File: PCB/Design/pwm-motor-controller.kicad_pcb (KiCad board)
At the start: 2 copper layers, 39 x 53.8 mm, 36 parts, among them J1 Screw_Terminal_01x02, J10 Conn_01x01, J2 Conn_01x01, J3 Conn_01x01, J4 Conn_01x01, J5 Conn_01x01, J6 Conn_01x01, J7 Conn_01x01, J8 Conn_01x01, J9 Conn_01x01, M1 Motor_DC, Q2 NMOS, Q3 MMBT2222A, Q4 Si2319CDS, Q5 NMOS, Q6 MMBT2222A, U1 LMC555xM

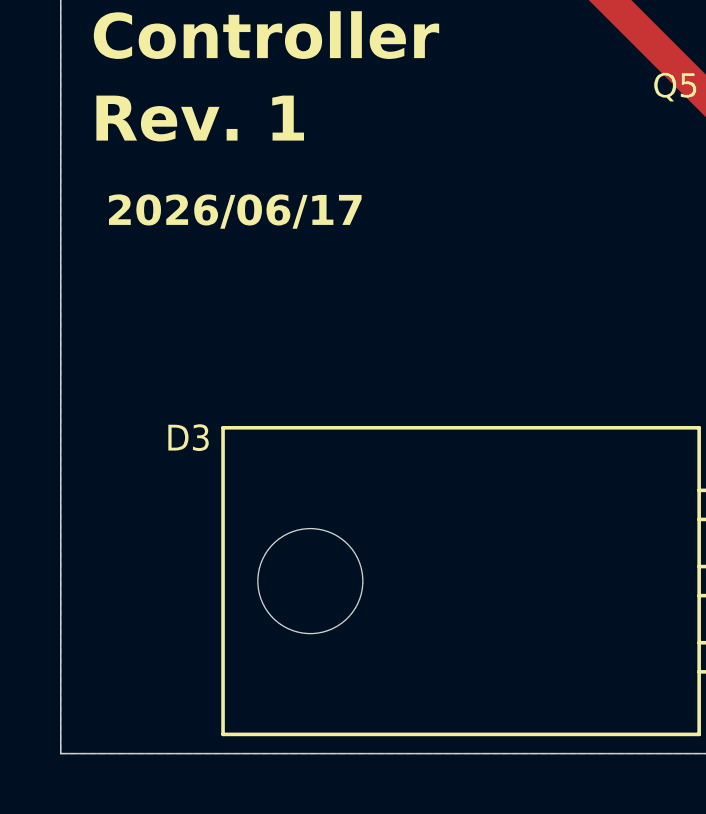
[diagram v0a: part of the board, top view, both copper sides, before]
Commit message: Added mounting holes
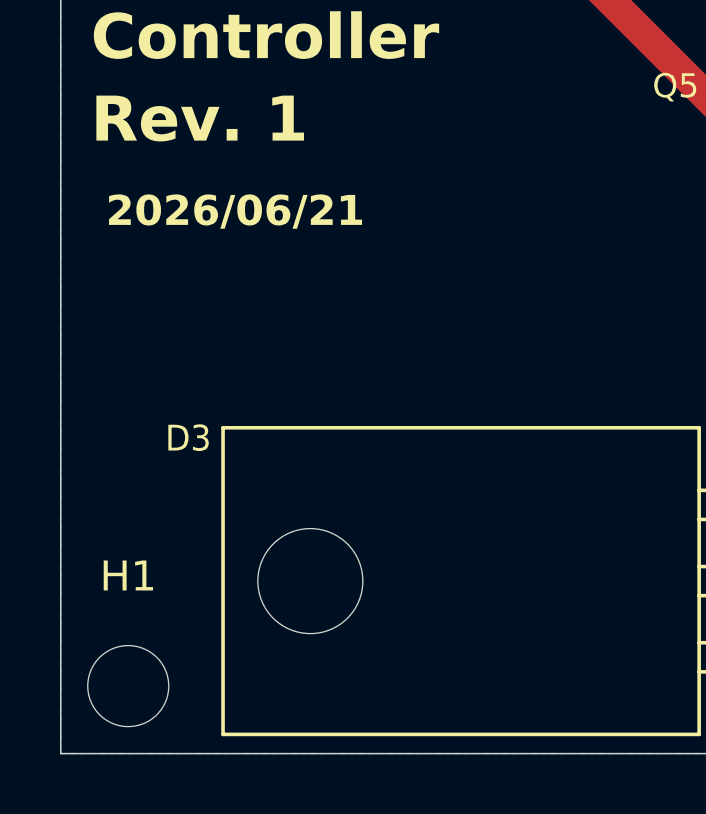
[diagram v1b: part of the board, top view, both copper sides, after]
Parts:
- added H1: MountingHole, MountingHole:MountingHole_2.7mm_M2.5, F.Cu at (198.8, 143.8)
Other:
- board text added: "2026/06/21"
- board text removed: "2026/06/17"
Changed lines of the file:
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@@
 		)
 	)
+	(footprint "MountingHole:MountingHole_2.7mm_M2.5"
+		(layer "F.Cu")
+		(at 198.75 143.75)
+		(descr "Mounting Hole 2.7mm, M2.5, no annular, generated by kicad-footprint-generator mountinghole.py")
+		(tags "mountinghole M2.5")
+		(property "Reference" "H1"
+			(at 0 -3.65 0)
+			(layer "F.SilkS")
+			(effects
+				(font
+					(size 1 1)
+					(thickness 0.15)
+				)
+			)
+		)
+		(property "Value" "MountingHole"
+			(at 0 3.65 0)
+			(layer "F.Fab")
+			(effects
+				(font
+					(size 1 1)
+					(thickness 0.15)
+				)
+			)
+		)
+		(property "Datasheet" "~"
+			(at 0 0 0)
+			(layer "F.Fab")
+			(hide yes)
+			(effects
+				(font
+					(size 1.27 1.27)
+					(thickness 0.15)
+				)
+			)
+		)
+		(property "Description" "Mounting Hole without connection"
+			(at 0 0 0)
+			(layer "F.Fab")
+			(hide yes)
+			(effects
+				(font
+					(size 1.27 1.27)
+					(thickness 0.15)
+				)
+			)
+		)
+		(property ki_fp_filters "MountingHole*")
+		(sheetname "/")
+		(sheetfile "pwm-motor-controller.kicad_sch")
+		(attr exclude_from_pos_files exclude_from_bom)
+		(fp_circle
+			(center 0 0)
+			(end 2.7 0)
+			(stroke
+				(width 0.15)
+				(type solid)
+			)
+			(fill no)
+			(layer "Cmts.User")
+		)
+		(fp_circle
+			(center 0 0)
+			(end 2.95 0)
+			(stroke
+				(width 0.05)
+				(type solid)
+			)
+			(fill no)
+			(layer "F.CrtYd")
+		)
+		(fp_text user "${REFERENCE}"
+			(at 0 0 0)
+			(layer "F.Fab")
+			(effects
+				(font
+					(size 1 1)
+					(thickness 0.15)
+				)
+			)
+		)
+		(pad "" np_thru_hole circle
+			(at 0 0)
+			(size 2.7 2.7)
+			(drill 2.7)
+			(layers "*.Cu" "*.Mask")
+		)
+		(embedded_fonts no)
+	)
 	(footprint "Resistor_SMD:R_0603_1608Metric"
 		(layer "F.Cu")
@@
 		)
 	)
-	(gr_text "2026/06/17"
+	(gr_text "2026/06/21"
 		(at 198 128.5 0)
 		(layer "F.SilkS")
